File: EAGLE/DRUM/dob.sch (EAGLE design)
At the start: 38 parts, among them U1 LM358, U2 LM358, U3 LM358

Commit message: 5.hét
Nyák terv kész, próbanyák forrasztása, kábelezés van hátra.
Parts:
- removed C10, C11, C12, C13: 100nF, resistor:C-EU050-035X075
- removed R10, R7, R8, R9: 10k, rcl:R-EU_0204/7
- renumbered ARDUINO to ATMEGA4809
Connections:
- net B0: no longer C10.2, R7.2
- net B1: no longer C11.2, R8.2
- net B2: no longer C12.2, R9.2
- net B3: no longer C13.2, R10.2
- net GND: now also ATMEGA4809.GND1; no longer ATMEGA4809.GND, C10.1, C11.1, C12.1, C13.1
- net VCC: no longer R10.1, R7.1, R8.1, R9.1
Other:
- moved on the sheet: C7, C8, C9, R12, R13, U1G3, U2G3, U3G3, X1-1, X1-2, X1-3, X1-4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

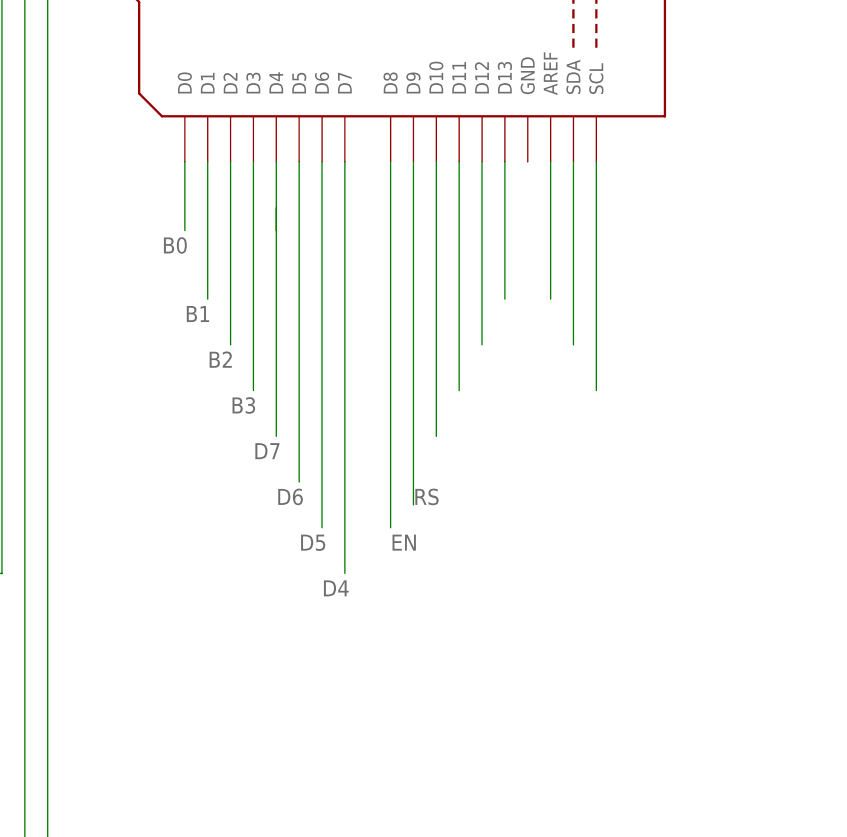
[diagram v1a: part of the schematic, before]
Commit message: LCD Gondok
Javítva a EAGLE kapcsolás. LCD még mindig nem jó.
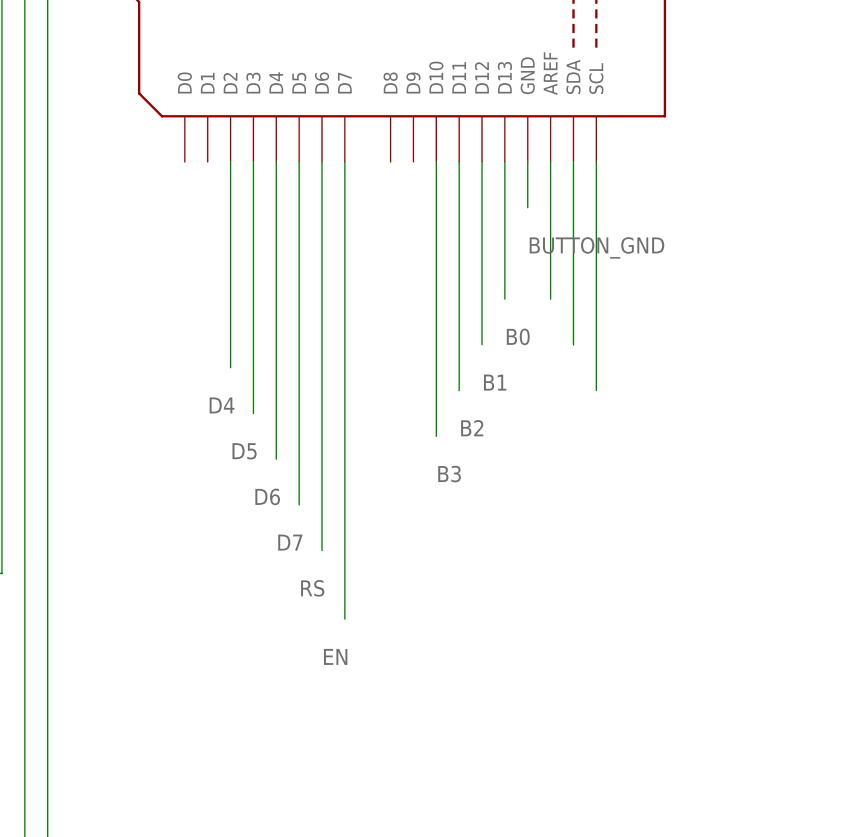
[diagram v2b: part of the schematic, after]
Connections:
- new net BUTTON_GND: ATMEGA4809.GND
- net B0: now also ATMEGA4809.D13; no longer ATMEGA4809.D0
- net B1: now also ATMEGA4809.D12; no longer ATMEGA4809.D1
- net B2: now also ATMEGA4809.D11; no longer ATMEGA4809.D2
- net B3: now also ATMEGA4809.D10; no longer ATMEGA4809.D3
- net D4: now also ATMEGA4809.D2; no longer ATMEGA4809.D7
- net D5: now also ATMEGA4809.D3; no longer ATMEGA4809.D6
- net D6: now also ATMEGA4809.D4; no longer ATMEGA4809.D5
- net D7: now also ATMEGA4809.D5
- net EN: now also ATMEGA4809.D7; no longer ATMEGA4809.D8
- net N$24: no longer ATMEGA4809.D10, ATMEGA4809.D11, ATMEGA4809.D12, ATMEGA4809.D13, ATMEGA4809.D4
- net RS: now also ATMEGA4809.D6; no longer ATMEGA4809.D9
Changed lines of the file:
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@@
 </segment>
 <segment>
-<wire x1="81.28" y1="-88.9" x2="81.28" y2="-134.62" width="0.1524" layer="91"/>
-<pinref part="ATMEGA4809" gate="G$1" pin="D7"/>
-<label x="78.74" y="-137.16" size="1.778" layer="95"/>
+<pinref part="ATMEGA4809" gate="G$1" pin="D2"/>
+<wire x1="68.58" y1="-88.9" x2="68.58" y2="-111.76" width="0.1524" layer="91"/>
+<label x="66.04" y="-116.84" size="1.778" layer="95"/>
 </segment>
 </net>
@@
 </segment>
 <segment>
-<wire x1="78.74" y1="-88.9" x2="78.74" y2="-129.54" width="0.1524" layer="91"/>
-<pinref part="ATMEGA4809" gate="G$1" pin="D6"/>
-<label x="76.2" y="-132.08" size="1.778" layer="95"/>
+<pinref part="ATMEGA4809" gate="G$1" pin="D3"/>
+<wire x1="71.12" y1="-88.9" x2="71.12" y2="-116.84" width="0.1524" layer="91"/>
+<label x="68.58" y="-121.92" size="1.778" layer="95"/>
 </segment>
 </net>
@@
 </segment>
 <segment>
-<pinref part="ATMEGA4809" gate="G$1" pin="D5"/>
-<wire x1="76.2" y1="-88.9" x2="76.2" y2="-124.46" width="0.1524" layer="91"/>
-<label x="73.66" y="-127" size="1.778" layer="95"/>
+<pinref part="ATMEGA4809" gate="G$1" pin="D4"/>
+<wire x1="73.66" y1="-88.9" x2="73.66" y2="-121.92" width="0.1524" layer="91"/>
+<label x="71.12" y="-127" size="1.778" layer="95"/>
 </segment>
 </net>
 <net name="N$24" class="0">
-<segment>
-<wire x1="73.66" y1="-88.9" x2="73.66" y2="-96.52" width="0.1524" layer="91"/>
-<pinref part="ATMEGA4809" gate="G$1" pin="D4"/>
-</segment>
-<segment>
-<wire x1="91.44" y1="-88.9" x2="91.44" y2="-119.38" width="0.1524" layer="91"/>
-<pinref part="ATMEGA4809" gate="G$1" pin="D10"/>
-</segment>
-<segment>
-<wire x1="93.98" y1="-88.9" x2="93.98" y2="-114.3" width="0.1524" layer="91"/>
-<pinref part="ATMEGA4809" gate="G$1" pin="D11"/>
-</segment>
-<segment>
-<wire x1="96.52" y1="-88.9" x2="96.52" y2="-109.22" width="0.1524" layer="91"/>
-<pinref part="ATMEGA4809" gate="G$1" pin="D12"/>
-</segment>
-<segment>
-<wire x1="99.06" y1="-88.9" x2="99.06" y2="-104.14" width="0.1524" layer="91"/>
-<pinref part="ATMEGA4809" gate="G$1" pin="D13"/>
-</segment>
 <segment>
 <wire x1="104.14" y1="-88.9" x2="104.14" y2="-104.14" width="0.1524" layer="91"/>
@@
 <net name="B1" class="0">
 <segment>
-<pinref part="ATMEGA4809" gate="G$1" pin="D1"/>
-<wire x1="66.04" y1="-88.9" x2="66.04" y2="-104.14" width="0.1524" layer="91"/>
-<label x="63.5" y="-106.68" size="1.778" layer="95"/>
-</segment>
-<segment>
 <pinref part="X1" gate="-2" pin="S"/>
 <wire x1="226.06" y1="-20.32" x2="210.82" y2="-20.32" width="0.1524" layer="91"/>
 <label x="208.28" y="-20.32" size="1.778" layer="95"/>
 </segment>
+<segment>
+<wire x1="96.52" y1="-88.9" x2="96.52" y2="-109.22" width="0.1524" layer="91"/>
+<pinref part="ATMEGA4809" gate="G$1" pin="D12"/>
+<label x="96.52" y="-114.3" size="1.778" layer="95"/>
+</segment>
 </net>
 <net name="B2" class="0">
-<segment>
-<pinref part="ATMEGA4809" gate="G$1" pin="D2"/>
-<wire x1="68.58" y1="-88.9" x2="68.58" y2="-109.22" width="0.1524" layer="91"/>
-<label x="66.04" y="-111.76" size="1.778" layer="95"/>
-</segment>
 <segment>
 <pinref part="X1" gate="-3" pin="S"/>
 <wire x1="259.08" y1="-20.32" x2="241.3" y2="-20.32" width="0.1524" layer="91"/>
 <label x="241.3" y="-20.32" size="1.778" layer="95"/>
+</segment>
+<segment>
+<wire x1="93.98" y1="-88.9" x2="93.98" y2="-114.3" width="0.1524" layer="91"/>
+<pinref part="ATMEGA4809" gate="G$1" pin="D11"/>
+<label x="93.98" y="-119.38" size="1.778" layer="95"/>
 </segment>
 </net>
@@
 </segment>
 <segment>
-<wire x1="73.66" y1="-93.98" x2="73.66" y2="-119.38" width="0.1524" layer="91"/>
-<label x="71.12" y="-121.92" size="1.778" layer="95"/>
+<pinref part="ATMEGA4809" gate="G$1" pin="D5"/>
+<wire x1="76.2" y1="-88.9" x2="76.2" y2="-127" width="0.1524" layer="91"/>
+<label x="73.66" y="-132.08" size="1.778" layer="95"/>
 </segment>
 </net>
@@
 </segment>
 <segment>
-<wire x1="86.36" y1="-88.9" x2="86.36" y2="-129.54" width="0.1524" layer="91"/>
-<pinref part="ATMEGA4809" gate="G$1" pin="D8"/>
-<label x="86.36" y="-132.08" size="1.778" layer="95"/>
+<pinref part="ATMEGA4809" gate="G$1" pin="D7"/>
+<wire x1="81.28" y1="-88.9" x2="81.28" y2="-139.7" width="0.1524" layer="91"/>
+<label x="78.74" y="-144.78" size="1.778" layer="95"/>
 </segment>
 </net>
@@
 </segment>
 <segment>
-<wire x1="88.9" y1="-88.9" x2="88.9" y2="-127" width="0.1524" layer="91"/>
-<pinref part="ATMEGA4809" gate="G$1" pin="D9"/>
-<label x="88.9" y="-127" size="1.778" layer="95"/>
+<pinref part="ATMEGA4809" gate="G$1" pin="D6"/>
+<wire x1="78.74" y1="-88.9" x2="78.74" y2="-132.08" width="0.1524" layer="91"/>
+<label x="76.2" y="-137.16" size="1.778" layer="95"/>
 </segment>
 </net>
 <net name="B0" class="0">
-<segment>
-<pinref part="ATMEGA4809" gate="G$1" pin="D0"/>
-<wire x1="63.5" y1="-88.9" x2="63.5" y2="-96.52" width="0.1524" layer="91"/>
-<label x="60.96" y="-99.06" size="1.778" layer="95"/>
-</segment>
 <segment>
 <pinref part="X1" gate="-1" pin="S"/>
@@
 <label x="172.72" y="-20.32" size="1.778" layer="95"/>
 </segment>
+<segment>
+<wire x1="99.06" y1="-88.9" x2="99.06" y2="-104.14" width="0.1524" layer="91"/>
+<pinref part="ATMEGA4809" gate="G$1" pin="D13"/>
+<label x="99.06" y="-109.22" size="1.778" layer="95"/>
+</segment>
 </net>
 <net name="B3" class="0">
-<segment>
-<pinref part="ATMEGA4809" gate="G$1" pin="D3"/>
-<wire x1="71.12" y1="-88.9" x2="71.12" y2="-114.3" width="0.1524" layer="91"/>
-<label x="68.58" y="-116.84" size="1.778" layer="95"/>
-</segment>
 <segment>
 <pinref part="X1" gate="-4" pin="S"/>
@@
 <label x="274.32" y="-20.32" size="1.778" layer="95"/>
 </segment>
+<segment>
+<wire x1="91.44" y1="-88.9" x2="91.44" y2="-119.38" width="0.1524" layer="91"/>
+<pinref part="ATMEGA4809" gate="G$1" pin="D10"/>
+<label x="91.44" y="-124.46" size="1.778" layer="95"/>
+</segment>
 </net>
+<net name="BUTTON_GND" class="0">
+<segment>
+<pinref part="ATMEGA4809" gate="G$1" pin="GND"/>
+<wire x1="101.6" y1="-88.9" x2="101.6" y2="-93.98" width="0.1524" layer="91"/>
+<label x="101.6" y="-99.06" size="1.778" layer="95"/>
+</segment>
+</net>
